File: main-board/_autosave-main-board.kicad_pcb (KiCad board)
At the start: 4 copper layers, 170.8 x 119.4 mm, 203 parts, among them IC10 SN74AXC4T774RSVR, IC13 TPS2121RUXR, IC15 SN74AXC4T774RSVR, IC16 SN74AXC4T774RSVR, IC2 SN74AXC4T774RSVR, IC3 SN74AXC4T774RSVR, IC4 SN74AXC4T774RSVR, J1 Conn_01x08, J12 Conn_01x01_Socket, J2 Conn_01x08, J20 Conn_01x01_Pin, J37 Conn_01x03, J4 Conn_01x08, J47 Barrel Jack, J5 Conn_01x08, J66 Conn_01x01_Socket, J68 Conn_02x02_Odd_Even, J70 Conn_01x07, J71 Conn_02x01, J72 Conn_01x07, J73 Conn_01x03, J74 Conn_Boaxial, J8 Conn_01x16, P2 USB Micro, SW1 SW_SPDT, SW2 SW_SPDT, SW3 SW_SPDT, SW5 SW_Push, U1 FT4232HL, U11 TS5A23159DGS, U12 TS5A23159DGS, U13 TS5A23159DGS, U14 TS5A23159DGS, U17 74AHC244, U2 W25Q128JWSIQ, U24 TCA9554ADBQR, U25 TCA9554ADBQR, U27 SI5351A-B-GTR, U28 TS5A23159DGS, U3 TLV75801PDBV, U31 74AHC244, U9 74AHCT1G08, X2 OK322532.768KJBA4SL, Y1 Crystal_GND24, Y2 NX3225GA-25.000M-STD-CRG-2

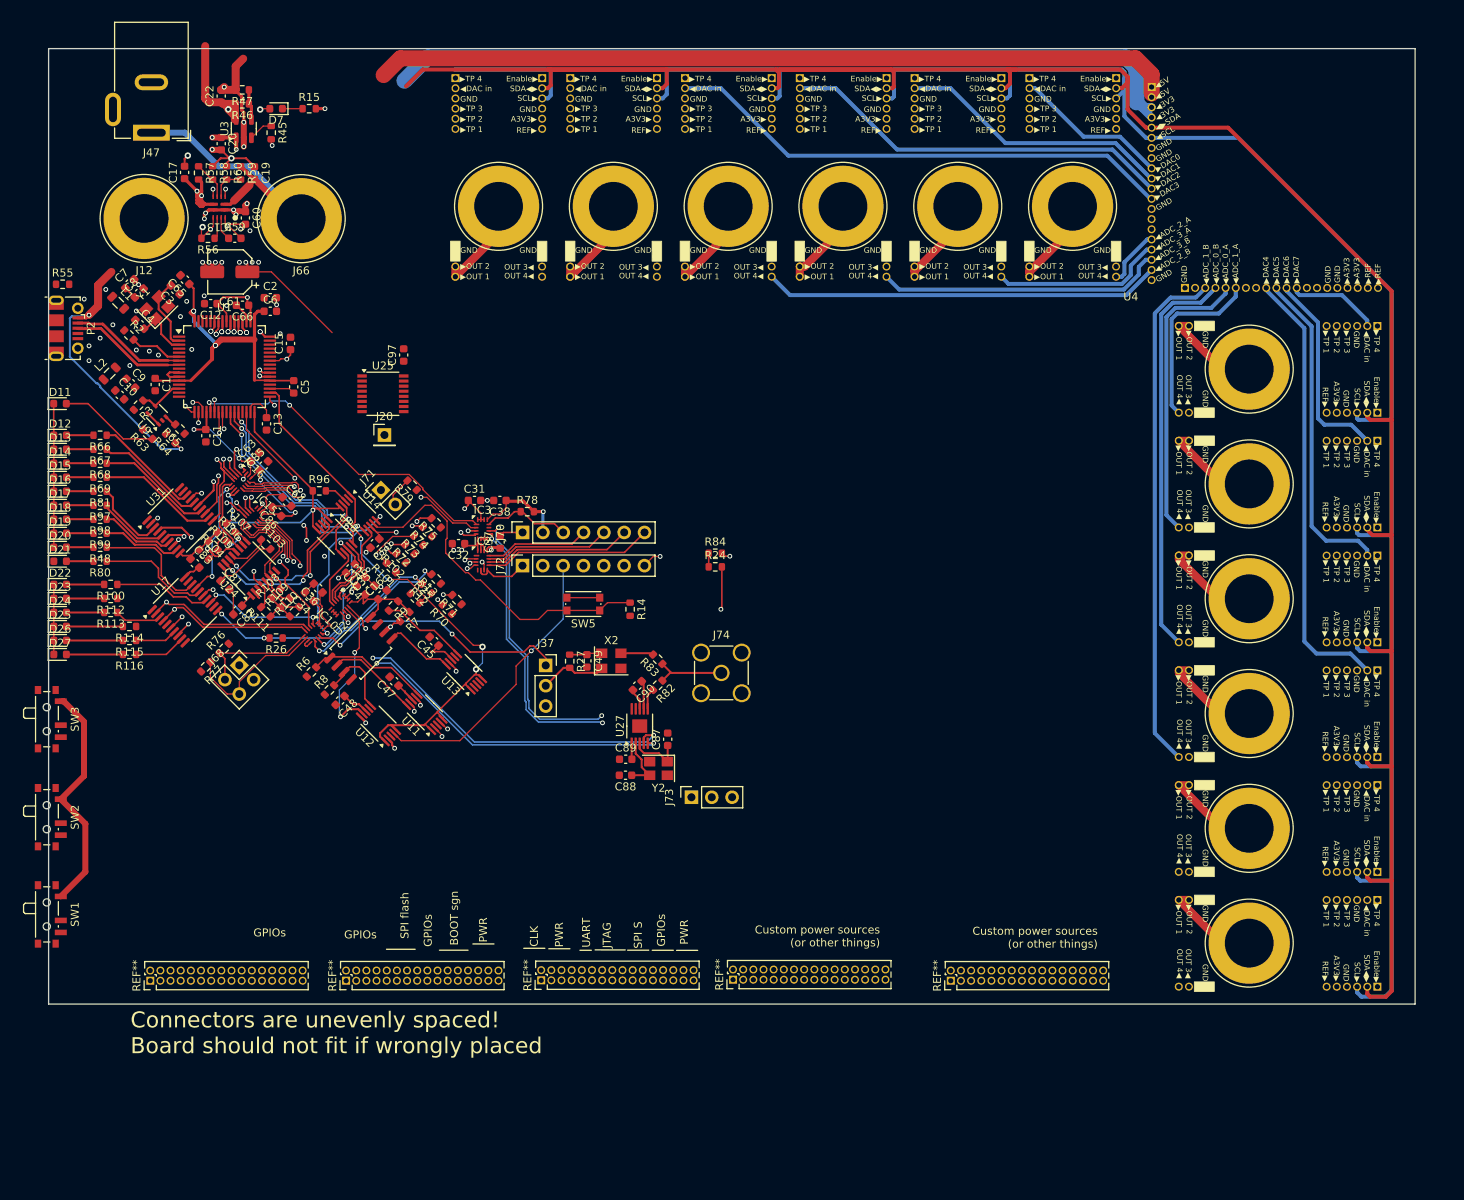
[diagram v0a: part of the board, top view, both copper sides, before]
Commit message: re-arranged adc/dac and routed to the cgs
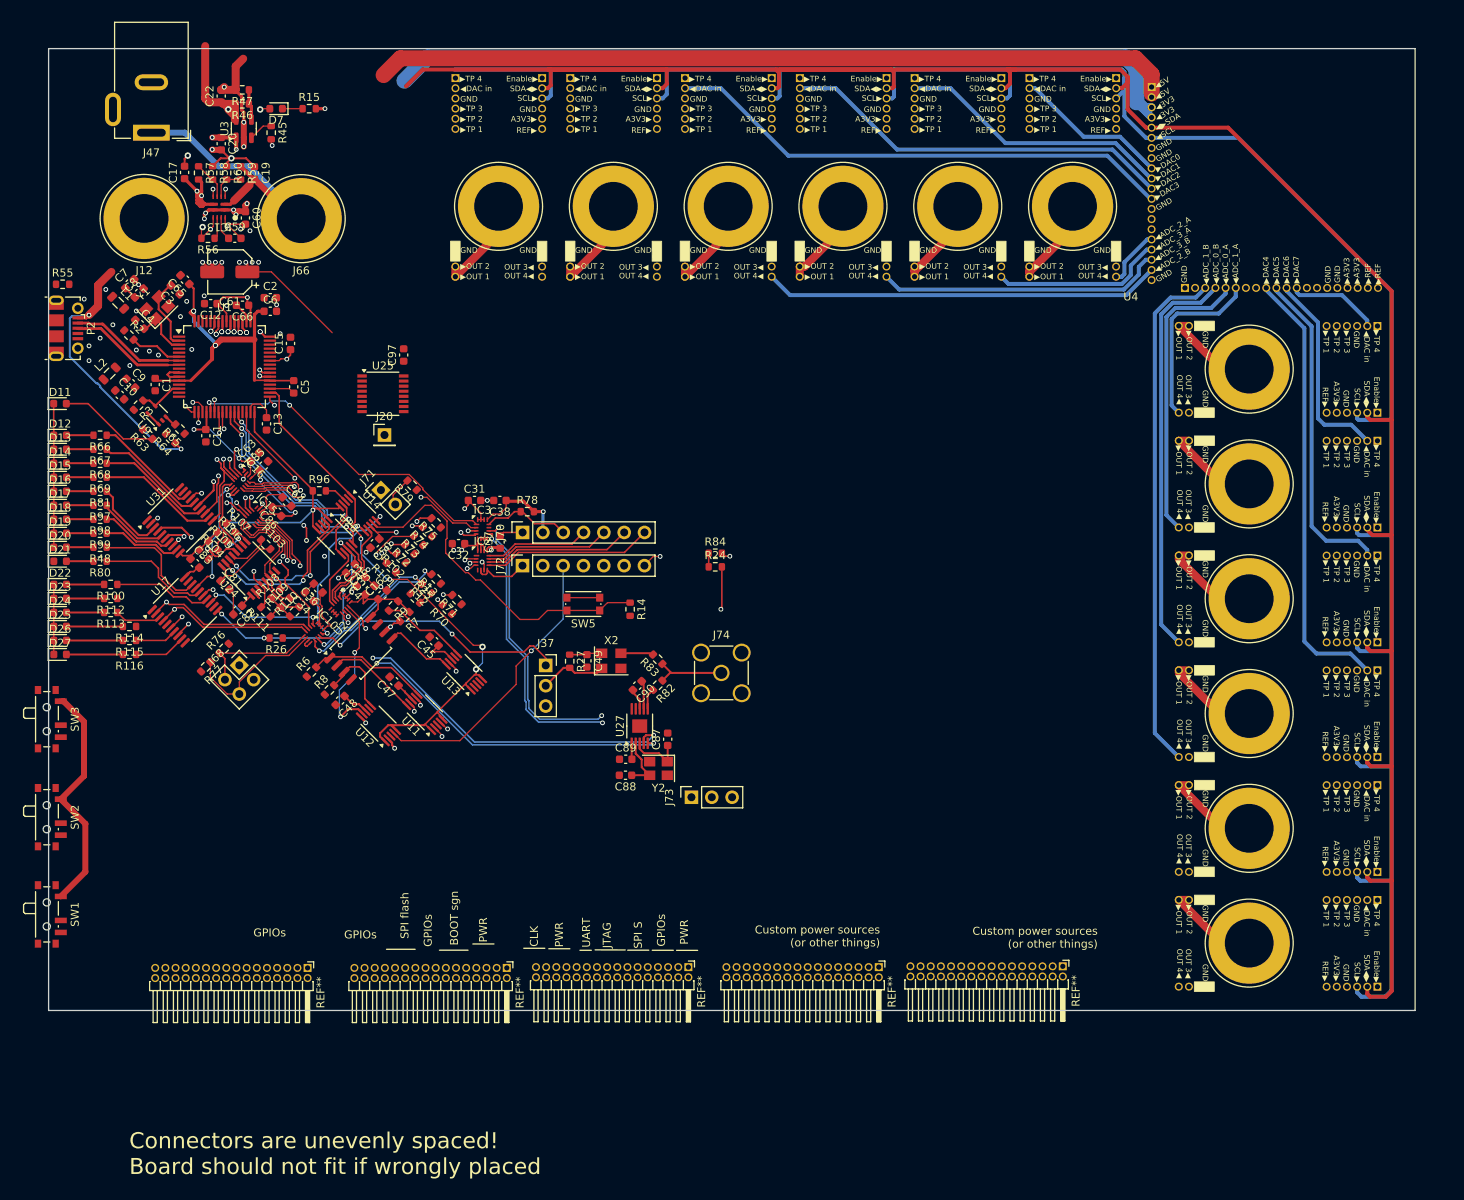
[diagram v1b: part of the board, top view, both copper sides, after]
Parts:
- REF** (x5): value PinHeader_2x16_P1.27mm_Vertical -> PinHeader_2x16_P1.27mm_Horizontal; footprint Connector_PinHeader_1.27mm:PinHeader_2x16_P1.27mm_Vertical -> Connector_PinHeader_1.27mm:PinHeader_2x16_P1.27mm_Horizontal
- moved REF** 20.2 mm to (127.5, 152.8), turned to -90 degrees
- moved REF** 19.7 mm to (102.6, 152.8), turned to -90 degrees
- moved REF** 18.5 mm to (150.2, 152.7), turned to -90 degrees
- moved REF** 18.3 mm to (174.0, 152.7), turned to -90 degrees
- moved REF** 14.1 mm to (197.0, 152.6), turned to -90 degrees
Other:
- board size 170.8 x 119.4 mm -> 170.8 x 120.2 mm
- board text removed: "Have one power per layer using the two central layers"
